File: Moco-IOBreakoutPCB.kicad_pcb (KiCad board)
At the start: 2 copper layers, 67.5 x 44 mm, 7 parts, among them J1 Conn_01x14, J2 Conn_01x14, J3 Conn_01x06, J4 Conn_01x06, J5 Conn_01x06

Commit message: final layout, no traces
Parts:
- moved REF** 2.50 mm to (177.5, 58.0)
- moved REF** 2.50 mm to (117.0, 58.0)
- moved J1 2.45 mm to (166.0, 58.0)
- moved J5 2.45 mm to (134.5, 57.9)
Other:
- board size 67.5 x 44 mm -> 67.5 x 45.5 mm
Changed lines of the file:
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@@
 	(footprint "MountingHole:MountingHole_3.2mm_M3"
 		(layer "F.Cu")
-		(at 177.5 55.5)
+		(at 177.5 58)
 		(descr "Mounting Hole 3.2mm, no annular, M3")
 		(tags "mounting hole 3.2mm no annular m3")
@@
 	(footprint "MountingHole:MountingHole_3.2mm_M3"
 		(layer "F.Cu")
-		(at 117 55.5)
+		(at 117 58)
 		(descr "Mounting Hole 3.2mm, no annular, M3")
 		(tags "mounting hole 3.2mm no annular m3")
@@
 	(footprint "UTSVT_Connectors:Molex_Microfit3.0_02x07_14-Pin-Vertical-PCB-Receptacle_447691401"
 		(layer "B.Cu")
-		(at 166 60.45 180)
+		(at 166 58 180)
 		(tags "447691401 ")
 		(property "Reference" "J1"
@@
 	(footprint "UTSVT_Connectors:Molex_Microfit3.0_02x03_6-Pin-Vertical-PCB-Receptacle_447690601"
 		(layer "B.Cu")
-		(at 134.5 60.399999 180)
+		(at 134.5 57.949999 180)
 		(tags "447690601 ")
 		(property "Reference" "J5"
@@
 	)
 	(gr_arc
-		(start 113.5 55)
-		(mid 114.37868 52.87868)
-		(end 116.5 52)
+		(start 113.5 53.469675)
+		(mid 114.37868 51.348355)
+		(end 116.5 50.469675)
 		(stroke
 			(width 0.2)
@@
 	)
 	(gr_line
-		(start 181 55.06065)
+		(start 181 53.530325)
 		(end 181 61.5)
 		(stroke
@@
 	(gr_line
 		(start 113.5 61.5)
-		(end 113.5 55)
+		(end 113.5 53.4697)
 		(stroke
 			(width 0.2)
@@
 	)
 	(gr_arc
-		(start 178 52.06065)
-		(mid 180.12132 52.93933)
-		(end 181 55.06065)
+		(start 178 50.530325)
+		(mid 180.12132 51.409005)
+		(end 181 53.530325)
 		(stroke
 			(width 0.2)
@@
 	)
 	(gr_line
-		(start 116.5 52)
-		(end 178 52.06065)
+		(start 116.5 50.469675)
+		(end 178 50.530325)
 		(stroke
 			(width 0.2)

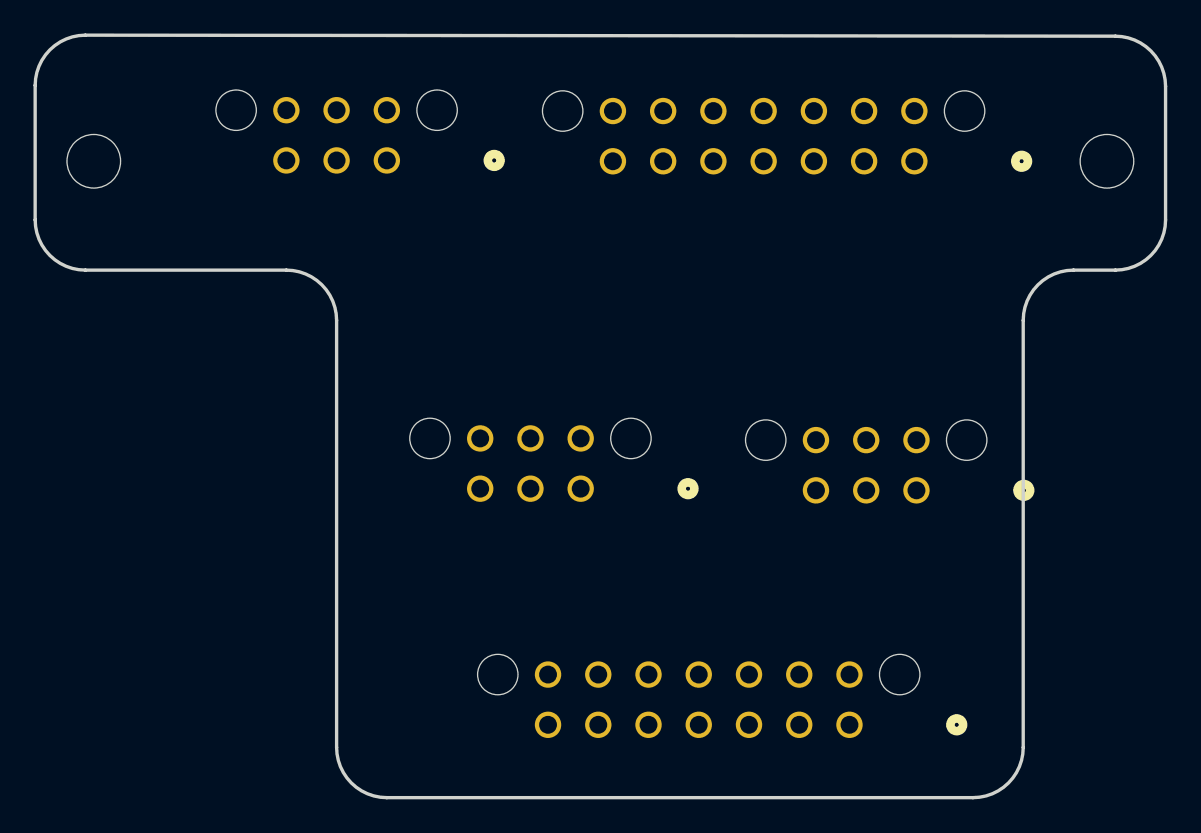
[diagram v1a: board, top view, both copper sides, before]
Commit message: ravi do the traces
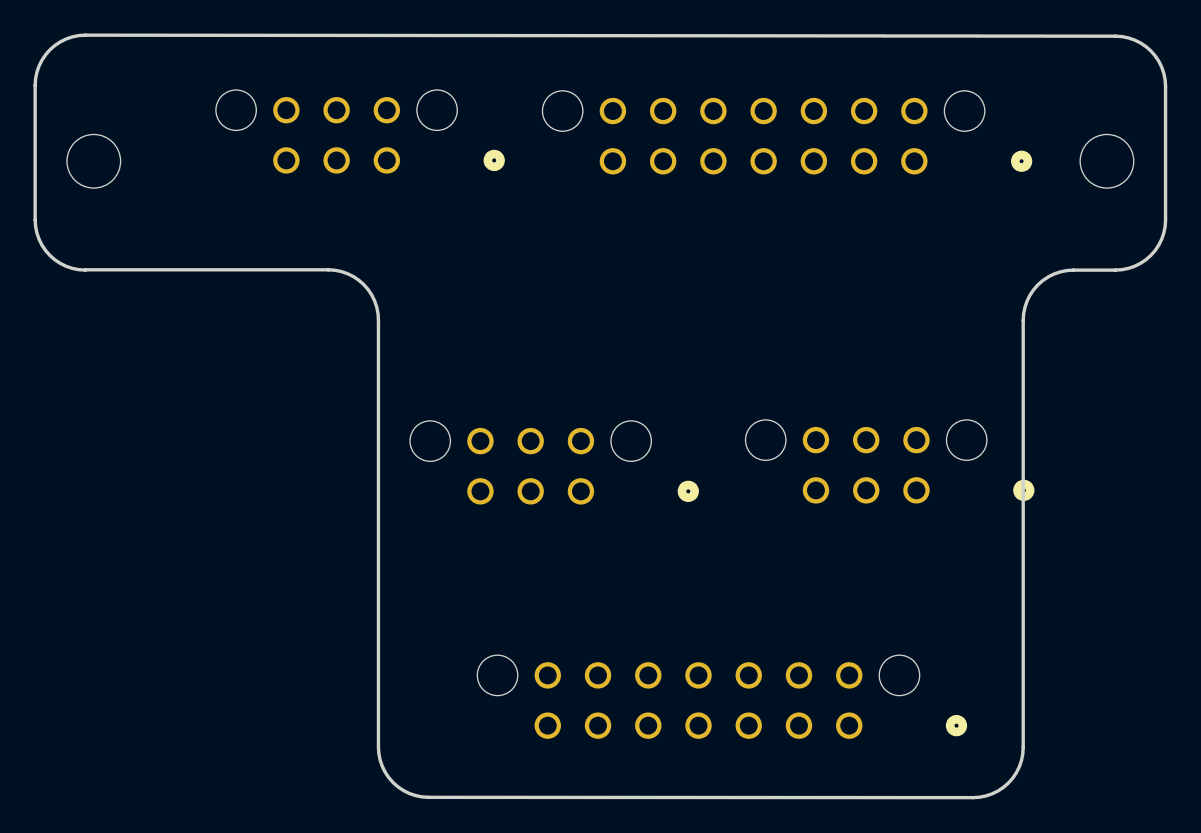
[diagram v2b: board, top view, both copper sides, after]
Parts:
- moved J4 0.16 mm to (146.1, 77.7)
- moved J2 0.05 mm to (162.1, 91.7)
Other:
- outline, holes or cut-outs redrawn
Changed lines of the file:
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@@
 	(footprint "UTSVT_Connectors:Molex_Microfit3.0_02x07_14-Pin-Vertical-PCB-Receptacle_447691401"
 		(layer "B.Cu")
-		(at 162.125 91.65 180)
+		(at 162.109994 91.699999 180)
 		(tags "447691401 ")
 		(property "Reference" "J2"
@@
 	(footprint "UTSVT_Connectors:Molex_Microfit3.0_02x03_6-Pin-Vertical-PCB-Receptacle_447690601"
 		(layer "B.Cu")
-		(at 146.075 77.55 180)
+		(at 146.089999 77.709999 180)
 		(tags "447690601 ")
 		(property "Reference" "J4"
@@
 	)
 	(gr_arc
-		(start 134.5 96)
-		(mid 132.37868 95.12132)
-		(end 131.5 93)
+		(start 136.99868 95.98132)
+		(mid 134.87736 95.10264)
+		(end 133.99868 92.98132)
 		(stroke
 			(width 0.2)
@@
 	)
 	(gr_arc
-		(start 128.5 64.5)
-		(mid 130.62132 65.37868)
-		(end 131.5 67.5)
+		(start 130.99868 64.48132)
+		(mid 133.12 65.36)
+		(end 133.99868 67.48132)
 		(stroke
 			(width 0.2)
@@
 	)
 	(gr_line
-		(start 116.5 64.5)
-		(end 128.5 64.5)
+		(start 116.5 64.481321)
+		(end 130.99868 64.481321)
 		(stroke
 			(width 0.2)
@@
 	)
 	(gr_line
-		(start 131.5 67.5)
-		(end 131.5 93)
+		(start 133.99868 67.48132)
+		(end 133.99868 92.98132)
 		(stroke
 			(width 0.2)
@@
 	(gr_line
 		(start 169.5 96)
-		(end 134.5 96)
+		(end 136.99868 95.981319)
 		(stroke
 			(width 0.2)
